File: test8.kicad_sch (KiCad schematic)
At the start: 3 parts, among them J1 Conn_01x02_Pin, U1 74HC165, U2 74HC165

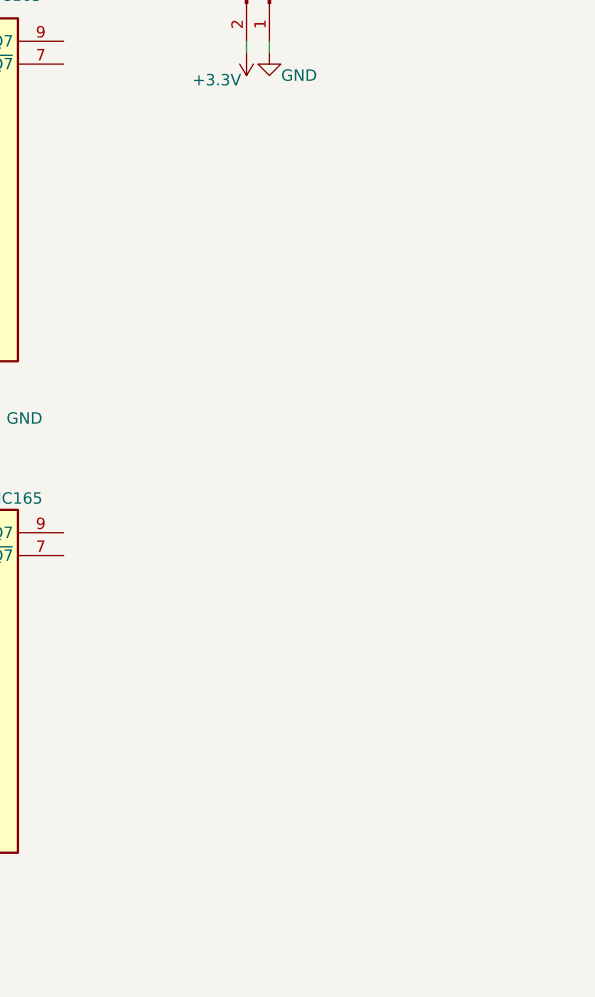
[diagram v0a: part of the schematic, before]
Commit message: esp32wrom process
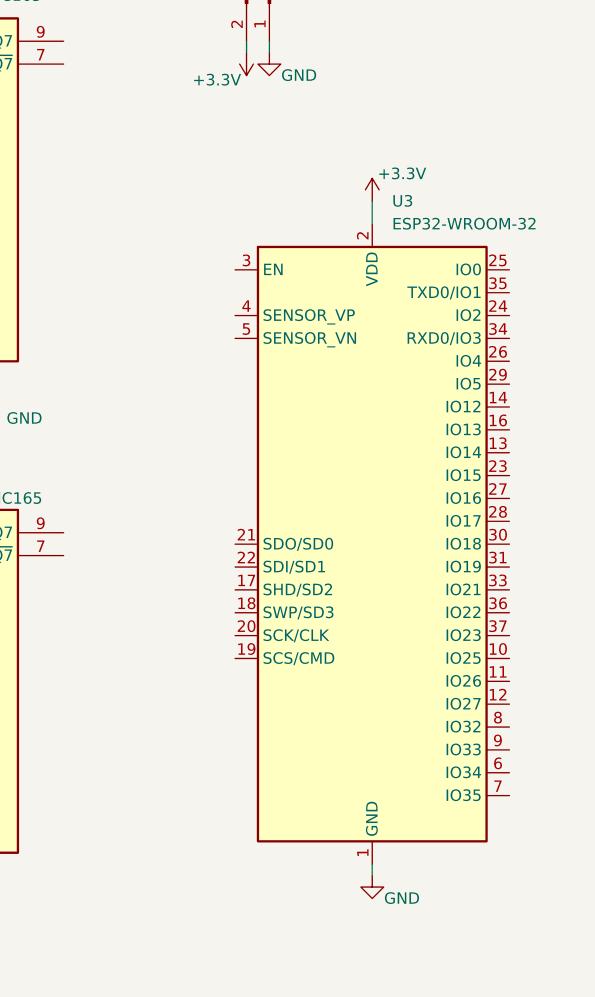
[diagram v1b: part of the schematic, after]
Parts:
- added U3: ESP32-WROOM-32, main:ESP32-WROOM-32, symbol main:ESP32-WROOM-32
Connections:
- net +3.3V: now also U3.2 (VDD)
- net GND: now also U3.1 (GND), U3.38 (GND)

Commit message: process
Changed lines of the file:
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@@
 	(wire
 		(pts
-			(xy 78.74 102.87) (xy 78.74 101.6)
+			(xy 125.73 78.74) (xy 125.73 81.28)
 		)
 		(stroke
@@
 	(wire
 		(pts
-			(xy 125.73 78.74) (xy 125.73 81.28)
+			(xy 125.73 152.4) (xy 125.73 153.67)
 		)
 		(stroke
@@
 	(wire
 		(pts
-			(xy 125.73 152.4) (xy 125.73 153.67)
+			(xy 78.74 50.8) (xy 78.74 53.34)
 		)
 		(stroke
@@
 	(wire
 		(pts
-			(xy 78.74 50.8) (xy 78.74 53.34)
+			(xy 111.76 60.96) (xy 111.76 62.23)
 		)
 		(stroke
@@
 	(wire
 		(pts
-			(xy 111.76 60.96) (xy 111.76 62.23)
+			(xy 81.28 101.6) (xy 78.74 101.6)
 		)
 		(stroke
@@
 	(wire
 		(pts
-			(xy 78.74 156.21) (xy 78.74 158.75)
+			(xy 80.01 156.21) (xy 78.74 156.21)
 		)
 		(stroke
@@
 	(wire
 		(pts
-			(xy 81.28 102.87) (xy 78.74 102.87)
+			(xy 114.3 60.96) (xy 114.3 62.23)
 		)
 		(stroke
@@
 		)
 	)
-	(wire
-		(pts
-			(xy 114.3 60.96) (xy 114.3 62.23)
-		)
-		(stroke
-			(width 0)
-			(type default)
-		)
-	)
 	(symbol
 		(lib_id "power:GND")
-		(at 78.74 158.75 0)
+		(at 80.01 156.21 90)
 		(unit 1)
 		(exclude_from_sim no)
@@
 		(fields_autoplaced yes)
 		(property "Reference" "#PWR05"
-			(at 78.74 165.1 0)
+			(at 86.36 156.21 0)
 			(effects
 				(font
@@
 		)
 		(property "Value" "GND"
-			(at 78.74 163.83 0)
-			(effects
-				(font
-					(size 1.27 1.27)
-				)
+			(at 83.82 156.2099 90)
+			(effects
+				(font
+					(size 1.27 1.27)
+				)
+				(justify right)
 			)
 		)
 		(property "Footprint" ""
-			(at 78.74 158.75 0)
+			(at 80.01 156.21 0)
 			(effects
 				(font
@@
 		)
 		(property "Datasheet" ""
-			(at 78.74 158.75 0)
+			(at 80.01 156.21 0)
 			(effects
 				(font
@@
 		)
 		(property "Description" "Power symbol creates a global label with name \"GND\" , ground"
-			(at 78.74 158.75 0)
+			(at 80.01 156.21 0)
 			(effects
 				(font
@@
 	(symbol
 		(lib_id "power:GND")
-		(at 125.73 153.67 0)
+		(at 125.73 153.67 90)
 		(unit 1)
 		(exclude_from_sim no)
@@
 		(dnp no)
 		(property "Reference" "#PWR08"
-			(at 125.73 160.02 0)
+			(at 132.08 153.67 0)
 			(effects
 				(font
@@
 		)
 		(property "Value" "GND"
-			(at 129.032 156.21 0)
+			(at 130.048 153.162 0)
 			(effects
 				(font
@@
 	(symbol
 		(lib_id "power:GND")
-		(at 81.28 102.87 90)
+		(at 81.28 101.6 90)
 		(unit 1)
 		(exclude_from_sim no)
@@
 		(fields_autoplaced yes)
 		(property "Reference" "#PWR02"
-			(at 87.63 102.87 0)
+			(at 87.63 101.6 0)
 			(effects
 				(font
@@
 		)
 		(property "Value" "GND"
-			(at 85.09 102.8699 90)
+			(at 85.09 101.5999 90)
 			(effects
 				(font
@@
 		)
 		(property "Footprint" ""
-			(at 81.28 102.87 0)
+			(at 81.28 101.6 0)
 			(effects
 				(font
@@
 		)
 		(property "Datasheet" ""
-			(at 81.28 102.87 0)
+			(at 81.28 101.6 0)
 			(effects
 				(font
@@
 		)
 		(property "Description" "Power symbol creates a global label with name \"GND\" , ground"
-			(at 81.28 102.87 0)
-			(effects
-				(font
+			(at 81.28 101.6 0)
+			(effects
+				(font

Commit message: xz
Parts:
- added U4, U5: 74HC595, Package_DIP:DIP-16_W7.62mm_LongPads, symbol 74xx:74HC595
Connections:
- net GND: now also U1.15 (~{CE}), U2.15 (~{CE}), U4.13 (~{OE}), U4.8 (GND), U5.13 (~{OE}), U5.8 (GND)
- net CS_165: now reaches U1.1 (~{PL})
- net CS_165: now also U2.1 (~{PL}), U3.5 (SENSOR_VN)
- net at U1.10 (DS): now also U2.9 (Q7)
- net CLK_165: now reaches U1.2 (CP)
- net CLK_165: now also U2.2 (CP), U3.30 (IO18)
- net MISO_165: now reaches U1.9 (Q7)
- net MISO_165: now also U3.31 (IO19)
- net at U3.13 (IO14): now also U4.11 (SRCLK), U5.11 (SRCLK)
- net at U3.16 (IO13): now also U4.14 (SER)
- net at U3.23 (IO15): now also U4.12 (RCLK), U5.12 (RCLK)
- new net: U4.9 (QH'), U5.14 (SER)
- new net +5V: U4.10 (~{SRCLR}), U4.16 (VCC), U5.10 (~{SRCLR}), U5.16 (VCC)
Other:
- moved on the sheet: J1, U3

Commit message: 595+165+topor
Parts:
- added J1, J2, J4, J5: Conn_01x10_Socket, main:PinHeader_2x05_P2.00mm_Vertical, symbol Connector:Conn_01x10_Socket
- J3: renamed from J1; footprint Connector_PinHeader_2.54mm:PinHeader_1x02_P2.54mm_Vertical -> main:PinHeader_1x02_P2.54mm_Vertical
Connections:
- net +3.3V: now also J1.9 (Pin_9), J2.9 (Pin_9)
- net +5V: now also J4.8 (Pin_8)
- net CLK_165: now also U1.1 (~{PL}); no longer U1.2 (CP)
- net CS_165: now also U1.2 (CP); no longer U1.1 (~{PL})
- net GND: now also J1.10 (Pin_10), J2.10 (Pin_10), J4.9 (Pin_9)
- net at U4.1 (QB): now also J4.2 (Pin_2)
- net at U4.15 (QA): now also J4.1 (Pin_1)
- net at U4.2 (QC): now also J4.3 (Pin_3)
- net at U4.3 (QD): now also J4.4 (Pin_4)
- net at U4.4 (QE): now also J4.5 (Pin_5)
- net at U4.5 (QF): now also J4.6 (Pin_6)
- net at U4.6 (QG): now also J4.7 (Pin_7)
- net at U4.7 (QH): now also J5.1 (Pin_1)
- net at U5.1 (QB): now also J5.3 (Pin_3)
- net at U5.15 (QA): now also J5.2 (Pin_2)
- net at U5.2 (QC): now also J5.4 (Pin_4)
- net at U5.3 (QD): now also J5.5 (Pin_5)
- net at U5.4 (QE): now also J5.6 (Pin_6)
- net at U5.5 (QF): now also J5.7 (Pin_7)
- net at U5.6 (QG): now also J5.8 (Pin_8)
- net at U5.7 (QH): now also J5.9 (Pin_9)
- net at U1.11 (D0): now also J1.1 (Pin_1)
- net at U1.12 (D1): now also J1.2 (Pin_2)
- net at U1.13 (D2): now also J1.3 (Pin_3)
- net at U1.14 (D3): now also J1.4 (Pin_4)
- net at U1.3 (D4): now also J1.5 (Pin_5)
- net at U1.4 (D5): now also J1.6 (Pin_6)
- net at U1.5 (D6): now also J1.7 (Pin_7)
- net at U1.6 (D7): now also J1.8 (Pin_8)
- net at U2.11 (D0): now also J2.1 (Pin_1)
- net at U2.12 (D1): now also J2.2 (Pin_2)
- net at U2.13 (D2): now also J2.3 (Pin_3)
- net at U2.14 (D3): now also J2.4 (Pin_4)
- net at U2.3 (D4): now also J2.5 (Pin_5)
- net at U2.4 (D5): now also J2.6 (Pin_6)
- net at U2.5 (D6): now also J2.7 (Pin_7)
- net at U2.6 (D7): now also J2.8 (Pin_8)

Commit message: вариант 1
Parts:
- added C1, C3, C5, C6, C7: C, Capacitor_SMD:C_0805_2012Metric, symbol Device:C
- added C2, C4: C_Polarized, Capacitor_THT:CP_Radial_D10.0mm_P5.00mm, symbol Device:C_Polarized
- added J4, J5, J6: Conn_01x03_Pin, main:PinSocket_1x03_P2.00mm_Vertical, symbol Connector:Conn_01x03_Pin
- added U3: AMS1117-3.3, Package_TO_SOT_SMD:SOT-223-3_TabPin2, symbol Regulator_Linear:AMS1117-3.3
- renumbered J4 to J7, J5 to J8, U3 to U4, U4 to U5, U5 to U6
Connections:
- net +3.3V: now also C3.2, C4.1, C5.2, C6.2, C7.2, J6.1 (Pin_1), U3.2 (VO); no longer J3.2 (Pin_2)
- net +5V: now also J3.1 (Pin_1), C1.2, C2.1, J5.1 (Pin_1), U3.3 (VI)
- net GND: now also J3.2 (Pin_2), C1.1, C2.2, C3.1, C4.2, C5.1, C6.1, C7.1, J4.3 (Pin_3), J5.3 (Pin_3), J6.3 (Pin_3), U3.1 (GND); no longer J3.1 (Pin_1)
- net H34P: now reaches U4.33 (IO21)
- net H34P: now also J5.2 (Pin_2)
- net at U4.34 (RXD0/IO3): now also J4.1 (Pin_1)
- net at U4.35 (TXD0/IO1): now also J4.2 (Pin_2)
- net RX433: now reaches U4.36 (IO22)
- net RX433: now also J6.2 (Pin_2)
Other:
- moved on the sheet: J3
